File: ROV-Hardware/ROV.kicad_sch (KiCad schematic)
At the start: 17 parts, among them J1 Screw_Terminal_01x02, J2 Screw_Terminal_01x02, J3 Screw_Terminal_01x04, SW1 SW_Wuerth_450301014042, U1 LM7812_TO220, U2 LM7805_TO220, U3 ESP32-S3-DEVKITC-1-N8R2, U4 MPU6050, U5 ZK-BM!, U6 ZK-BM!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

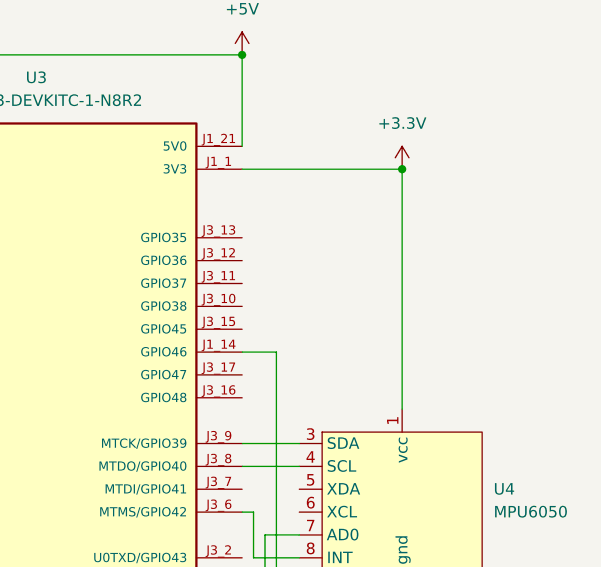
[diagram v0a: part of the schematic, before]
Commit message: Here I added GM-MS5837
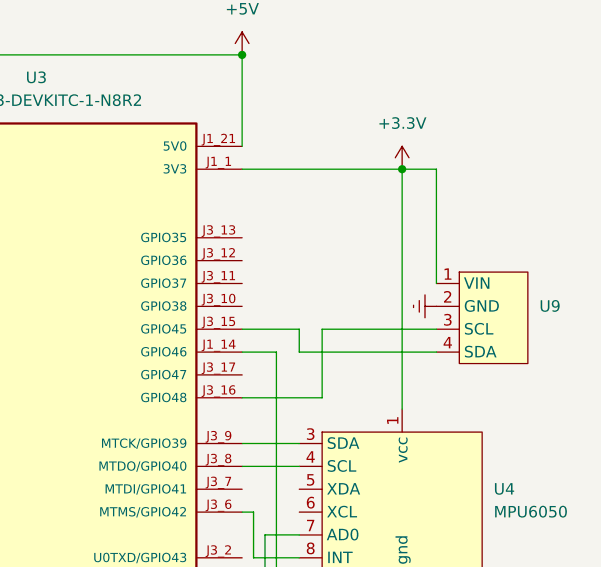
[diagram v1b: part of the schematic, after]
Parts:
- added U9: ~, Connector_PinHeader_2.54mm:PinHeader_1x04_P2.54mm_Vertical, symbol MPU6050:GY-MS5837
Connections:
- net +3.3V: now also U9.1 (VIN)
- net GND: now also U9.2 (GND)
- net at U3.J3_15 (GPIO45): now also U9.4 (SDA)
- net at U3.J3_16 (GPIO48): now also U9.3 (SCL)
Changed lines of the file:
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@@
+	(wire
+		(pts
+			(xy 252.73 83.82) (xy 252.73 96.52)
+		)
+		(stroke
+			(width 0)
+			(type default)
+		)
+	)
 	(wire
 		(pts
@@
 	(wire
 		(pts
+			(xy 237.49 101.6) (xy 231.14 101.6)
+		)
+		(stroke
+			(width 0)
+			(type default)
+		)
+	)
+	(wire
+		(pts
+			(xy 240.03 101.6) (xy 240.03 109.22)
+		)
+		(stroke
+			(width 0)
+			(type default)
+		)
+	)
+	(wire
+		(pts
 			(xy 173.99 137.16) (xy 185.42 137.16)
 		)
@@
 	(wire
 		(pts
+			(xy 240.03 109.22) (xy 231.14 109.22)
+		)
+		(stroke
+			(width 0)
+			(type default)
+		)
+	)
+	(wire
+		(pts
 			(xy 231.14 83.82) (xy 248.92 83.82)
 		)
@@
 	(wire
 		(pts
+			(xy 252.73 104.14) (xy 237.49 104.14)
+		)
+		(stroke
+			(width 0)
+			(type default)
+		)
+	)
+	(wire
+		(pts
 			(xy 173.99 144.78) (xy 234.95 144.78)
 		)
@@
 	(wire
 		(pts
+			(xy 252.73 101.6) (xy 240.03 101.6)
+		)
+		(stroke
+			(width 0)
+			(type default)
+		)
+	)
+	(wire
+		(pts
 			(xy 137.16 81.28) (xy 121.92 81.28)
 		)
@@
 	(wire
 		(pts
+			(xy 252.73 83.82) (xy 248.92 83.82)
+		)
+		(stroke
+			(width 0)
+			(type default)
+		)
+	)
+	(wire
+		(pts
 			(xy 121.92 81.28) (xy 121.92 83.82)
+		)
+		(stroke
+			(width 0)
+			(type default)
+		)
+	)
+	(wire
+		(pts
+			(xy 237.49 104.14) (xy 237.49 101.6)
 		)
 		(stroke
@@
 	)
 	(symbol
+		(lib_id "power:GNDREF")
+		(at 252.73 99.06 270)
+		(unit 1)
+		(exclude_from_sim no)
+		(in_bom yes)
+		(on_board yes)
+		(dnp no)
+		(property "Reference" "#PWR015"
+			(at 246.38 99.06 0)
+			(effects
+				(font
+					(size 1.27 1.27)
+				)
+				(hide yes)
+			)
+		)
+		(property "Value" "GNDREF"
+			(at 251.206 104.902 0)
+			(effects
+				(font
+					(size 1.27 1.27)
+				)
+				(hide yes)
+			)
+		)
+		(property "Footprint" ""
+			(at 252.73 99.06 0)
+			(effects
+				(font
+					(size 1.27 1.27)
+				)
+				(hide yes)
+			)
+		)
+		(property "Datasheet" ""
+			(at 252.73 99.06 0)
+			(effects
+				(font
+					(size 1.27 1.27)
+				)
+				(hide yes)
+			)
+		)
+		(property "Description" "Power symbol creates a global label with name \"GNDREF\" , reference supply ground"
+			(at 252.73 99.06 0)
+			(effects
+				(font
+					(size 1.27 1.27)
+				)
+				(hide yes)
+			)
+		)
+		(pin "1"
+		)
+		(instances
+			(project "ROV"
+				(path "/df7a457f-e553-4b1a-9143-cdb39e42e745"
+					(reference "#PWR015")
+					(unit 1)
+				)
+			)
+		)
+	)
+	(symbol
 		(lib_id "power:+12V")
 		(at 55.88 76.2 0)
@@
 					(unit 1)
 				)
+			)
+		)
+	)
+	(symbol
+		(lib_id "MPU6050:GY-MS5837")
+		(at 259.08 97.79 0)
+		(unit 1)
+		(exclude_from_sim no)
+		(in_bom yes)
+		(on_board yes)
+		(dnp no)
+		(fields_autoplaced yes)
+		(property "Reference" "U9"
+			(at 264.16 99.0599 0)
+			(effects
+				(font
+					(size 1.27 1.27)
+				)
+				(justify left)
+			)
+		)
+		(property "Value" "~"
+			(at 264.16 101.5999 0)
+			(effects
+				(font
+					(size 1.27 1.27)
+				)
+				(justify left)
+			)
+		)
+		(property "Footprint" "Connector_PinHeader_2.54mm:PinHeader_1x04_P2.54mm_Vertical"
+			(at 259.08 97.79 0)
+			(effects
+				(font
+					(size 1.27 1.27)
+				)
+				(hide yes)
+			)
+		)
+		(property "Datasheet" ""
+			(at 259.08 97.79 0)
+			(effects
+				(font
+					(size 1.27 1.27)
+				)
+				(hide yes)
+			)
+		)
+		(property "Description" ""
+			(at 259.08 97.79 0)
+			(effects
+				(font
+					(size 1.27 1.27)
+				)
+				(hide yes)
+			)
+		)
+		(pin "4"
+		)
+		(pin "3"
+		)
+		(pin "2"
+		)
+		(pin "1"
+		)
+		(instances
+			(project ""
+				(path "/df7a457f-e553-4b1a-9143-cdb39e42e745"
+					(reference "U9")
+					(unit 1)
+				)

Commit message: refresh
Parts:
- added D2, D3, D4, D5: LED, LED_THT:LED_D3.0mm, symbol Device:LED
- added F2: fuse, Fuse:Fuseholder_Clip-5x20mm_Schurter_CQM_Inline_P20.60x5.00mm_D1.00mm_Horizontal, symbol Device:Fuse
- added R1, R2, R3, R4: R, Resistor_THT:R_Axial_DIN0204_L3.6mm_D1.6mm_P5.08mm_Horizontal, symbol Device:R
- C1, C2, C3: value C_Polarized -> capacitor
- F1: value Fuse -> fuse
- J1: value Screw_Terminal_01x02 -> T-block; footprint TerminalBlock:TerminalBlock_MaiXu_MX126-5.0-02P_1x02_P5.00mm -> Connector_AMASS:AMASS_XT60-F_1x02_P7.20mm_Vertical
- J2: value Screw_Terminal_01x02 -> T-block
- SW1: value SW_Wuerth_450301014042 -> switch
- U1: value LM7812_TO220 -> LM7812
- U2: value LM7805_TO220 -> LM7805
- U5, U6, U7: value ZK-BM! -> ZK-BM1
- U8: value ~ -> A4988
- U9: value ~ -> GY-MS5837
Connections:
- net GND: now also R1.1, R2.1, R3.1, R4.1
- net Power1: no longer names the net of F1.2, SW1.3 (A)
- net Power1: now also D5.2 (A)
- net Power2: no longer names the net of C1.1, SW1.1 (B), U1.1 (VI), U2.1 (VI)
- net Power2: now also D2.2 (A)
- net Power3: no longer names the net of C2.1, U2.3 (VO)
- net Power3: now also D3.2 (A), F2.1; no longer D1.2 (A)
- net Power4: no longer names the net of C3.1, J2.2 (Pin_2), U1.3 (VO), U8.9 (VMOT)
- net Power4: now also D4.2 (A)
- new net: D2.1 (K), R1.2
- new net: D5.1 (K), R4.2
- new net: D4.1 (K), R3.2
- new net: D3.1 (K), R2.2
- new net: D1.2 (A), F2.2
- no-connect marks 3 -> 23

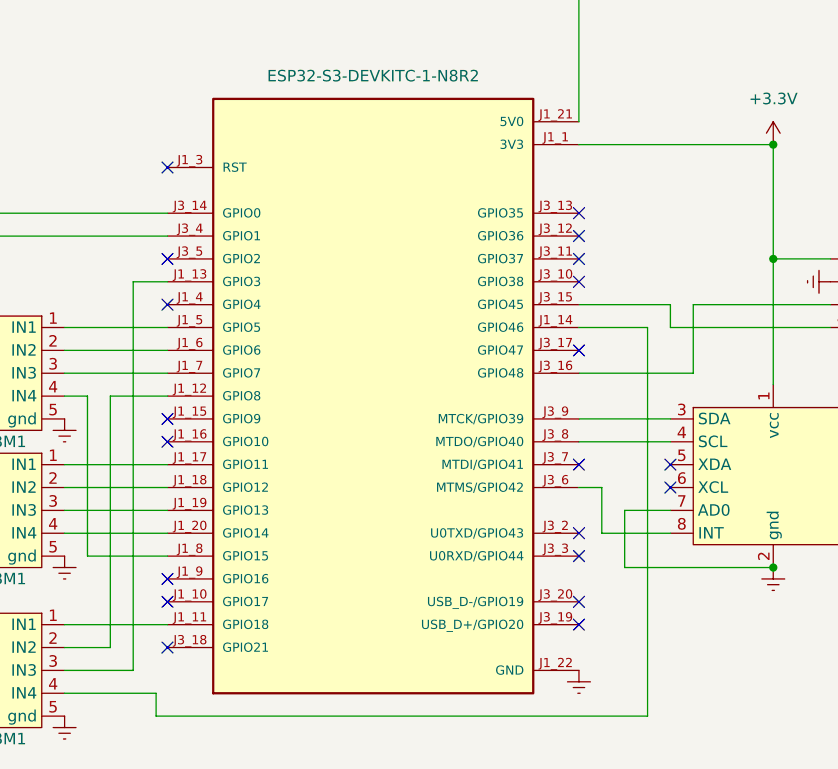
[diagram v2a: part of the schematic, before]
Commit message: editing power and grounding tracks
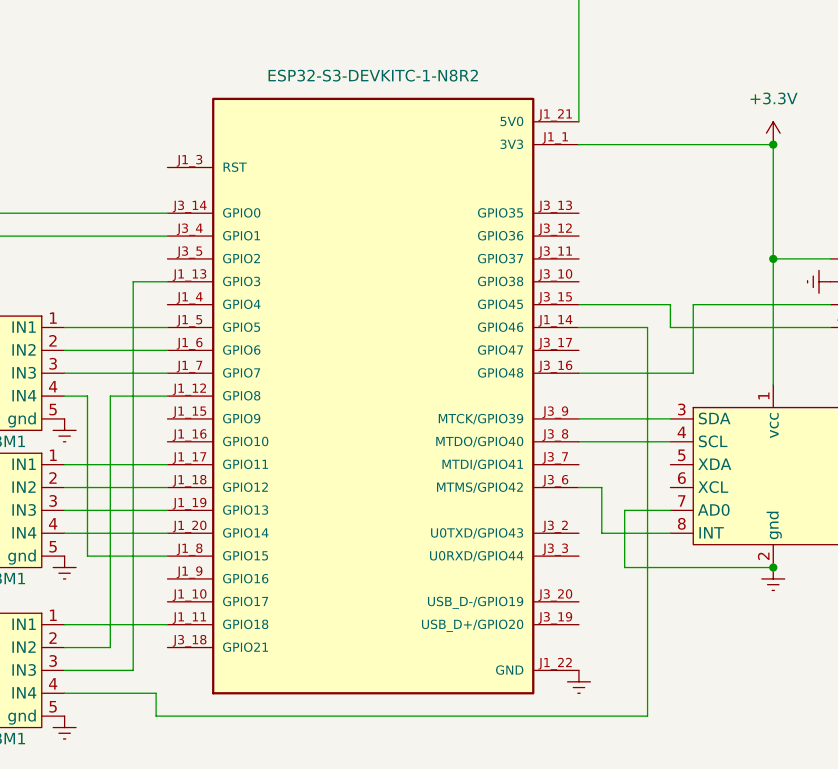
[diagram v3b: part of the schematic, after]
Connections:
- no-connect marks 23 -> 3
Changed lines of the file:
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@@
-	)
-	(no_connect
-		(at 213.36 66.04)
-	)
-	(no_connect
-		(at 213.36 93.98)
-	)
-	(no_connect
-		(at 167.64 106.68)
-	)
-	(no_connect
-		(at 167.64 91.44)
-	)
-	(no_connect
-		(at 167.64 60.96)
-	)
-	(no_connect
-		(at 213.36 71.12)
-	)
-	(no_connect
-		(at 213.36 109.22)
-	)
-	(no_connect
-		(at 167.64 76.2)
-	)
-	(no_connect
-		(at 213.36 73.66)
-	)
-	(no_connect
-		(at 213.36 101.6)
 	)
 	(no_connect
@@
 	)
 	(no_connect
-		(at 223.52 93.98)
-	)
-	(no_connect
 		(at 107.95 86.36)
-	)
-	(no_connect
-		(at 167.64 109.22)
-	)
-	(no_connect
-		(at 167.64 71.12)
 	)
 	(no_connect
 		(at 107.95 88.9)
 	)
-	(no_connect
-		(at 213.36 68.58)
-	)
-	(no_connect
-		(at 167.64 88.9)
-	)
-	(no_connect
-		(at 213.36 81.28)
-	)
-	(no_connect
-		(at 167.64 114.3)
-	)
-	(no_connect
-		(at 213.36 111.76)
-	)
-	(no_connect
-		(at 223.52 96.52)
-	)
-	(no_connect
-		(at 213.36 104.14)
-	)
 	(wire

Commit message: water sensor
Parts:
- added U10: ~, Connector_PinHeader_2.54mm:PinHeader_1x03_P2.54mm_Vertical, symbol MPU6050:water
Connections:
- net +3.3V: now also U10.2 (+)
- net GND: now also U10.3 (-)
- net at U3.J1_4 (GPIO4): now also U10.1 (S)
- net at U3.J3_10 (GPIO38): now also U4.4 (SCL)
- net at U3.J3_11 (GPIO37): now also U4.3 (SDA)
- net at U3.J3_14 (GPIO0): no longer U8.7 (STEP)
- net at U3.J3_5 (GPIO2): now also U8.7 (STEP)
- net at U3.J3_8 (MTDO/GPIO40): no longer U4.4 (SCL)
- net at U3.J3_9 (MTCK/GPIO39): no longer U4.3 (SDA)
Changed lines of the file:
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@@
 	(wire
 		(pts
+			(xy 161.29 76.2) (xy 167.64 76.2)
+		)
+		(stroke
+			(width 0)
+			(type default)
+		)
+	)
+	(wire
+		(pts
 			(xy 88.9 35.56) (xy 96.52 35.56)
 		)
@@
 	(wire
 		(pts
+			(xy 234.95 58.42) (xy 247.65 58.42)
+		)
+		(stroke
+			(width 0)
+			(type default)
+		)
+	)
+	(wire
+		(pts
 			(xy 67.31 49.53) (xy 67.31 48.26)
 		)
@@
 	(wire
 		(pts
-			(xy 142.24 68.58) (xy 142.24 106.68)
+			(xy 138.43 68.58) (xy 138.43 106.68)
 		)
 		(stroke
@@
 	(wire
 		(pts
+			(xy 247.65 55.88) (xy 247.65 48.26)
+		)
+		(stroke
+			(width 0)
+			(type default)
+		)
+	)
+	(wire
+		(pts
 			(xy 223.52 76.2) (xy 213.36 76.2)
 		)
@@
 	(wire
 		(pts
+			(xy 223.52 91.44) (xy 215.9 91.44)
+		)
+		(stroke
+			(width 0)
+			(type default)
+		)
+	)
+	(wire
+		(pts
 			(xy 156.21 96.52) (xy 167.64 96.52)
 		)
@@
 	(wire
 		(pts
-			(xy 139.7 66.04) (xy 167.64 66.04)
+			(xy 215.9 73.66) (xy 213.36 73.66)
 		)
 		(stroke
@@
 	(wire
 		(pts
-			(xy 139.7 104.14) (xy 105.41 104.14)
+			(xy 140.97 71.12) (xy 167.64 71.12)
 		)
 		(stroke
@@
 	(wire
 		(pts
-			(xy 166.37 121.92) (xy 166.37 119.38)
+			(xy 140.97 109.22) (xy 105.41 109.22)
 		)
 		(stroke
@@
 	(wire
 		(pts
-			(xy 142.24 68.58) (xy 167.64 68.58)
+			(xy 166.37 121.92) (xy 166.37 119.38)
 		)
 		(stroke
@@
 	(wire
 		(pts
-			(xy 116.84 43.18) (xy 116.84 50.8)
+			(xy 138.43 68.58) (xy 167.64 68.58)
 		)
 		(stroke
@@
 	(wire
 		(pts
-			(xy 223.52 99.06) (xy 218.44 99.06)
+			(xy 116.84 43.18) (xy 116.84 50.8)
 		)
 		(stroke
@@
 	(wire
 		(pts
-			(xy 67.31 48.26) (xy 68.58 48.26)
+			(xy 223.52 99.06) (xy 218.44 99.06)
 		)
 		(stroke
@@
 	(wire
 		(pts
-			(xy 234.95 71.12) (xy 241.3 71.12)
+			(xy 67.31 48.26) (xy 68.58 48.26)
 		)
 		(stroke
@@
 	(wire
 		(pts
-			(xy 213.36 91.44) (xy 223.52 91.44)
+			(xy 234.95 71.12) (xy 241.3 71.12)
 		)
 		(stroke
@@
 	(wire
 		(pts
+			(xy 218.44 88.9) (xy 218.44 71.12)
+		)
+		(stroke
+			(width 0)
+			(type default)
+		)
+	)
+	(wire
+		(pts
 			(xy 67.31 52.07) (xy 67.31 53.34)
 		)
@@
 	(wire
 		(pts
-			(xy 105.41 104.14) (xy 105.41 99.06)
+			(xy 105.41 109.22) (xy 105.41 99.06)
 		)
 		(stroke
@@
 	(wire
 		(pts
+			(xy 223.52 88.9) (xy 218.44 88.9)
+		)
+		(stroke
+			(width 0)
+			(type default)
+		)
+	)
+	(wire
+		(pts
 			(xy 76.2 48.26) (xy 77.47 48.26)
 		)
@@
 	(wire
 		(pts
-			(xy 142.24 106.68) (xy 106.68 106.68)
+			(xy 138.43 106.68) (xy 106.68 106.68)
 		)
 		(stroke
@@
 	(wire
 		(pts
+			(xy 140.97 71.12) (xy 140.97 109.22)
+		)
+		(stroke
+			(width 0)
+			(type default)
+		)
+	)
+	(wire
+		(pts
 			(xy 105.41 99.06) (xy 107.95 99.06)
 		)
@@
 	(wire
 		(pts
+			(xy 161.29 48.26) (xy 161.29 76.2)
+		)
+		(stroke
+			(width 0)
+			(type default)
+		)
+	)
+	(wire
+		(pts
 			(xy 156.21 93.98) (xy 167.64 93.98)
 		)
@@
 	(wire
 		(pts
+			(xy 218.44 71.12) (xy 213.36 71.12)
+		)
+		(stroke
+			(width 0)
+			(type default)
+		)
+	)
+	(wire
+		(pts
 			(xy 163.83 73.66) (xy 167.64 73.66)
 		)
@@
 	(wire
 		(pts
-			(xy 88.9 66.04) (xy 99.06 66.04)
+			(xy 247.65 48.26) (xy 161.29 48.26)
 		)
 		(stroke
@@
 	(wire
 		(pts
-			(xy 156.21 78.74) (xy 167.64 78.74)
+			(xy 215.9 91.44) (xy 215.9 73.66)
 		)
 		(stroke
@@
 	(wire
 		(pts
-			(xy 144.78 35.56) (xy 143.51 35.56)
+			(xy 88.9 66.04) (xy 99.06 66.04)
 		)
 		(stroke
@@
 	(wire
 		(pts
-			(xy 156.21 99.06) (xy 167.64 99.06)
+			(xy 156.21 78.74) (xy 167.64 78.74)
 		)
 		(stroke
@@
 	(wire
 		(pts
-			(xy 161.29 86.36) (xy 167.64 86.36)
+			(xy 144.78 35.56) (xy 143.51 35.56)
 		)
 		(stroke
@@
 	(wire
 		(pts
-			(xy 139.7 66.04) (xy 139.7 104.14)
+			(xy 156.21 99.06) (xy 167.64 99.06)
+		)
+		(stroke
+			(width 0)
+			(type default)
+		)
+	)
+	(wire
+		(pts
+			(xy 161.29 86.36) (xy 167.64 86.36)
 		)
 		(stroke
@@
 	(wire
 		(pts
-			(xy 223.52 88.9) (xy 213.36 88.9)
-		)
-		(stroke
-			(width 0)
-			(type default)
-		)
-	)
-	(wire
-		(pts
 			(xy 76.2 30.48) (xy 128.27 30.48)
 		)
@@
 	)
 	(symbol
+		(lib_id "MPU6050:water")
+		(at 252.73 58.42 0)
+		(unit 1)
+		(exclude_from_sim no)
+		(in_bom yes)
+		(on_board yes)
+		(dnp no)
+		(fields_autoplaced yes)
+		(property "Reference" "U10"
+			(at 256.54 57.1499 0)
+			(effects
+				(font
+					(size 1.27 1.27)
+				)
+				(justify left)
+			)
+		)
+		(property "Value" "~"
+			(at 256.54 59.6899 0)
+			(effects
+				(font
+					(size 1.27 1.27)
+				)
+				(justify left)
+			)
+		)
+		(property "Footprint" "Connector_PinHeader_2.54mm:PinHeader_1x03_P2.54mm_Vertical"
+			(at 252.73 58.42 0)
+			(effects
+				(font
+					(size 1.27 1.27)
+				)
+				(hide yes)
+			)
+		)
+		(property "Datasheet" ""
+			(at 252.73 58.42 0)
+			(effects
+				(font
+					(size 1.27 1.27)
+				)
+				(hide yes)
+			)
+		)
+		(property "Description" ""
+			(at 252.73 58.42 0)
+			(effects
+				(font
+					(size 1.27 1.27)
+				)
+				(hide yes)
+			)
+		)
+		(pin "1"
+		)
+		(pin "2"
+		)
+		(pin "3"
+		)
+		(instances
+			(project ""
+				(path "/df7a457f-e553-4b1a-9143-cdb39e42e745"
+					(reference "U10")
+					(unit 1)
+				)
+			)
+		)
+	)
+	(symbol
 		(lib_id "Device:R")
 		(at 123.19 54.61 0)
@@
 					(unit 1)
 				)
+			)
+		)
+	)
+	(symbol
+		(lib_id "power:GNDREF")
+		(at 247.65 60.96 270)
+		(unit 1)
+		(exclude_from_sim no)
+		(in_bom yes)
+		(on_board yes)
+		(dnp no)
+		(property "Reference" "#PWR016"
+			(at 241.3 60.96 0)
+			(effects
+				(font
+					(size 1.27 1.27)
+				)
+				(hide yes)
+			)
+		)
+		(property "Value" "GNDREF"
+			(at 246.126 66.802 0)
+			(effects
+				(font
+					(size 1.27 1.27)
+				)
+				(hide yes)
+			)
+		)
+		(property "Footprint" ""
+			(at 247.65 60.96 0)
+			(effects
+				(font
+					(size 1.27 1.27)
+				)
+				(hide yes)
+			)
+		)
+		(property "Datasheet" ""
+			(at 247.65 60.96 0)
+			(effects
+				(font
+					(size 1.27 1.27)
+				)
+				(hide yes)
+			)
+		)
+		(property "Description" "Power symbol creates a global label with name \"GNDREF\" , reference supply ground"
+			(at 247.65 60.96 0)
+			(effects
+				(font
+					(size 1.27 1.27)
+				)
+				(hide yes)
+			)
+		)
+		(pin "1"
+		)
+		(instances
+			(project "ROV"
+				(path "/df7a457f-e553-4b1a-9143-cdb39e42e745"
+					(reference "#PWR016")
+					(unit 1)
+				)

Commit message: hight current
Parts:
- removed C3: capacitor, Capacitor_THT:CP_Radial_D5.0mm_P2.50mm, symbol Device:C_Polarized
- removed D4, D5: LED, LED_THT:LED_D3.0mm, symbol Device:LED
- removed J2: T-block, TerminalBlock:TerminalBlock_MaiXu_MX126-5.0-02P_1x02_P5.00mm, symbol Connector:Screw_Terminal_01x02
- removed R3, R4: R, Resistor_THT:R_Axial_DIN0204_L3.6mm_D1.6mm_P5.08mm_Horizontal, symbol Device:R
- removed SW1: switch, Button_Switch_THT:SW_Slide-03_Wuerth-WS-SLTV_10x2.5x6.4_P2.54mm, symbol Switch:SW_Wuerth_450301014042
- removed U1: LM7812, Package_TO_SOT_THT:TO-220-3_Vertical, symbol Regulator_Linear:LM7812_TO220
- added F3, F4, F5: fuse, Fuse:Fuseholder_Clip-5x20mm_Schurter_CQM_Inline_P20.60x5.00mm_D1.00mm_Horizontal, symbol Device:Fuse
- added J2: Screw_Terminal_01x04, TerminalBlock:TerminalBlock_MaiXu_MX126-5.0-04P_1x04_P5.00mm, symbol Connector:Screw_Terminal_01x04
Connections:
- net GND: now also C1.1, J2.1 (Pin_1); no longer C1.2
- net at U3.J3_4 (GPIO1): now also U8.7 (STEP); no longer U8.8 (DIR)
- net at U3.J3_5 (GPIO2): now also U8.8 (DIR); no longer U8.7 (STEP)
- net at U8.9 (VMOT): now also C1.2, D2.2 (A), F1.2, U2.1 (VI), F3.1, F4.1, F5.1
- new net: F5.2, J2.4 (Pin_4)
- new net: F4.2, J2.3 (Pin_3)
- new net: F3.2, J2.2 (Pin_2)
- no-connect marks 3 -> 0
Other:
- moved on the sheet: U10
